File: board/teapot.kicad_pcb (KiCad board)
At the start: 2 copper layers, 50 x 50 mm, 15 parts, among them P1 BATT, P2 SMA, Q1 TEPT4400, U1 TLV61225, U2 microusb-b, U3 RFM69W, U4 STM32L052K8, U5 HTU21D, U6 MS5637, U7 SWD, U8 TPS79333DBVR

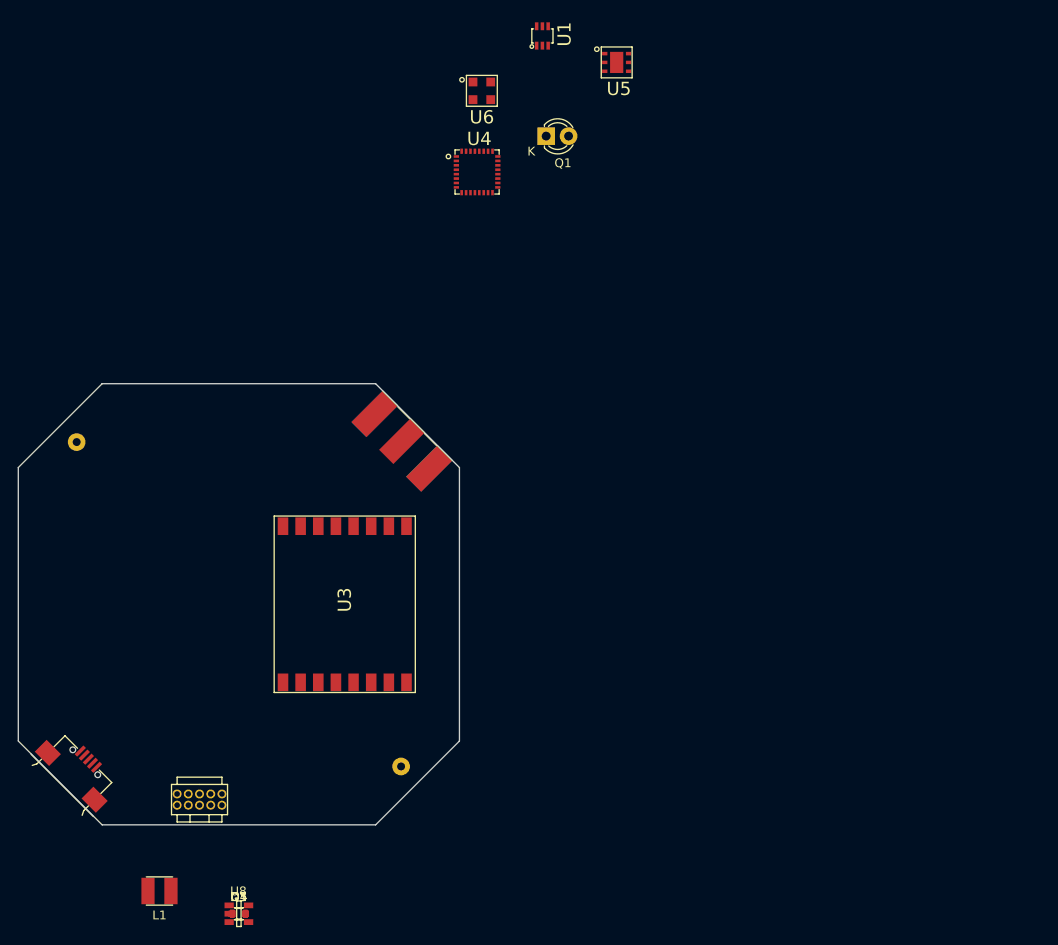
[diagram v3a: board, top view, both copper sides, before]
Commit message: Fixed a couple of footprint derps
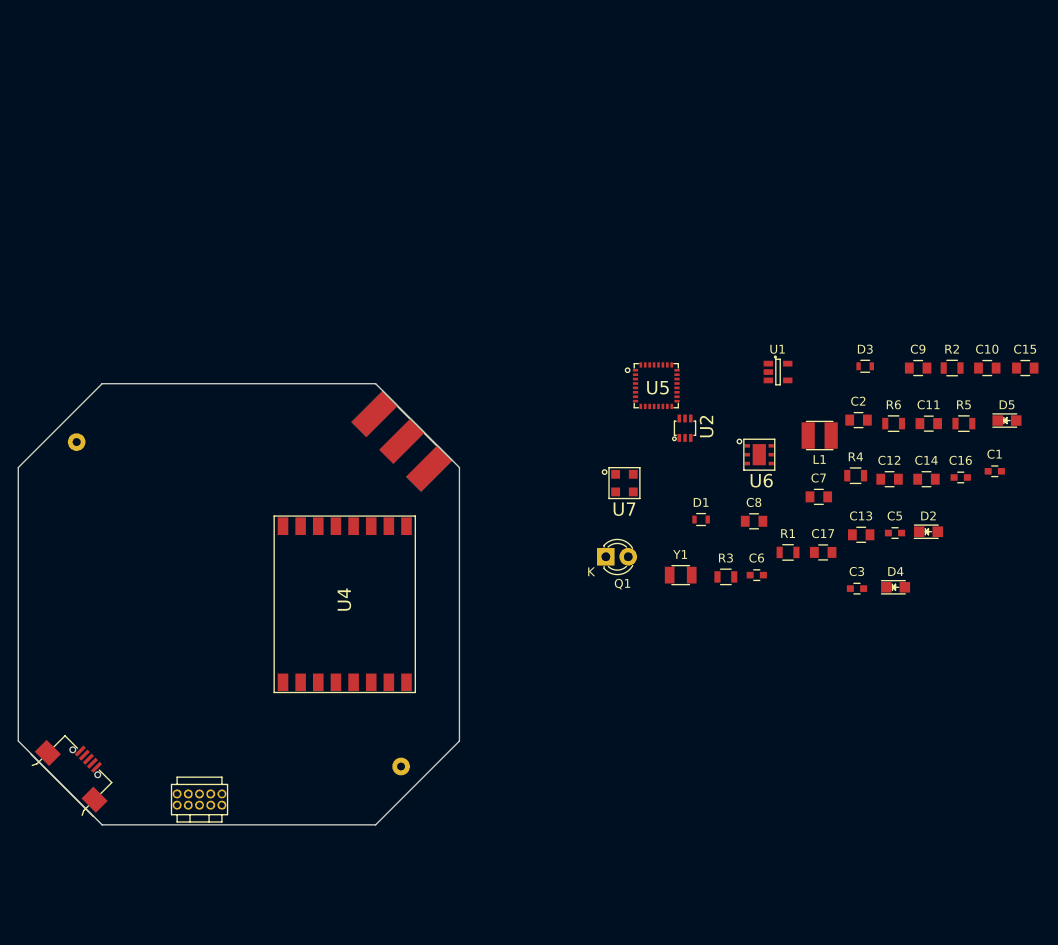
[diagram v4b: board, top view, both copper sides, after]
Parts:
- added C10: 100n, Capacitors_SMD:C_0805, F.Cu at (211.8, 86.2)
- added C11: 100n, Capacitors_SMD:C_0805, F.Cu at (205.2, 92.5)
- added C12: 1u, Capacitors_SMD:C_0805, F.Cu at (200.8, 98.8)
- added C13: 100n, Capacitors_SMD:C_0805, F.Cu at (197.5, 105.1)
- added C14: 100n, Capacitors_SMD:C_0805, F.Cu at (204.9, 98.8)
- added C15: 100n, Capacitors_SMD:C_0805, F.Cu at (216.1, 86.2)
- added C16: 10u, Capacitors_SMD:C_0603, F.Cu at (208.8, 98.6)
- added C17: 100n, Capacitors_SMD:C_0805, F.Cu at (193.2, 107.1)
- added C2: 100n, Capacitors_SMD:C_0805, F.Cu at (197.2, 92.1)
- added C3: 10u, Capacitors_SMD:C_0603, F.Cu at (197.1, 111.2)
- added C5: 10u, Capacitors_SMD:C_0603, F.Cu at (201.4, 104.9)
- added C6: 10u, Capacitors_SMD:C_0603, F.Cu at (185.7, 109.7)
- added C7: 100n, Capacitors_SMD:C_0805, F.Cu at (192.7, 100.8)
- added C8: 15p, Capacitors_SMD:C_0805, F.Cu at (185.4, 103.6)
- added C9: 15p, Capacitors_SMD:C_0805, F.Cu at (204.0, 86.2)
- added D2: RED, LEDs:LED-0805, F.Cu at (205.2, 104.8)
- added D4: GREEN, LEDs:LED-0805, F.Cu at (201.4, 111.1)
- added D5: YELLOW, LEDs:LED-0805, F.Cu at (214.1, 92.2)
- added R1: 1k, Resistors_SMD:R_0805, F.Cu at (189.2, 107.1)
- added R2: 10k, Resistors_SMD:R_0805, F.Cu at (207.8, 86.2)
- added R3: 10k, Resistors_SMD:R_0805, F.Cu at (182.2, 109.9)
- added R4: 1k, Resistors_SMD:R_0805, F.Cu at (196.9, 98.4)
- added R5: 1k, Resistors_SMD:R_0805, F.Cu at (209.2, 92.5)
- added R6: 10k, Resistors_SMD:R_0805, F.Cu at (201.2, 92.5)
- added Y1: 32.768k, footprints:XTAL_1206, F.Cu at (177.1, 109.7)
- moved C1 99.3 mm to (212.7, 97.9)
- moved D3 94.3 mm to (198.0, 86.0)
- moved L1 90.9 mm to (192.8, 93.9)
- moved U1 86.6 mm to (188.1, 86.7)
- moved D1 68.9 mm to (179.4, 103.4)
- moved Q1 48.2 mm to (168.6, 107.6)
- moved U2 47.3 mm to (177.6, 93.0)
- moved U7 47.3 mm to (170.7, 99.3)
- moved U6 47.3 mm to (186.0, 96.0)
- moved U5 31.6 mm to (174.3, 88.2)
- renumbered D4 to D1, D5 to D3, U8 to U1, U1 to U2, U2 to U3, U3 to U4, U4 to U5, U5 to U6, U6 to U7, U7 to U8
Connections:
- Q1 pad 1: (no net) -> /LIGHT
- U2 pad 2: (no net) -> Net-(C3-Pad1)
- U5 pad 2: (no net) -> Net-(C9-Pad1)
- U5 pad 3: (no net) -> Net-(C8-Pad1)
- U5 pad 5: (no net) -> Net-(C12-Pad1)

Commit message: Power consumption calculations
Resolves #5, resolves #2
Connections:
- net /LIGHT renamed /LIGHT_SENSE
- Q1 pad 2: +3V3 -> (no net)
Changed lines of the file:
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@@
 (kicad_pcb (version 4) (host pcbnew 4.0.1-3.201512150931+6195~38~ubuntu14.04.1-stable)
   (general
-    (links 91)
-    (no_connects 91)
+    (links 90)
+    (no_connects 90)
     (area 101.924999 87.924999 152.075001 138.075001)
     (thickness 1.6)
@@
   (net 19 "Net-(D4-Pad1)")
   (net 20 "Net-(D5-Pad1)")
-  (net 21 /LIGHT)
+  (net 21 /LIGHT_SENSE)
   (net_class Default "This is the default net class."
     (clearance 0.2)
@@
     (add_net /I2C_SCK)
     (add_net /I2C_SDA)
-    (add_net /LIGHT)
+    (add_net /LIGHT_SENSE)
     (add_net /SWCLK)
     (add_net /SWDIO)
@@
     )
     (pad 1 thru_hole rect (at 0 0 90) (size 2 2) (drill 1.00076) (layers *.Cu *.Mask F.SilkS)
-      (net 21 /LIGHT))
-    (pad 2 thru_hole circle (at 2.54 0) (size 2 2) (drill 1.00076) (layers *.Cu *.Mask F.SilkS)
-      (net 1 +3V3))
+      (net 21 /LIGHT_SENSE))
+    (pad 2 thru_hole circle (at 2.54 0) (size 2 2) (drill 1.00076) (layers *.Cu *.Mask F.SilkS))
     (model LEDs.3dshapes/LED-3MM.wrl
       (at (xyz 0.05 0 0))
@@
     (fp_line (start -0.6 -0.875) (end 0.6 -0.875) (layer F.SilkS) (width 0.15))
     (pad 1 smd rect (at -0.95 0) (size 0.7 1.3) (layers F.Cu F.Paste F.Mask)
-      (net 21 /LIGHT))
+      (net 21 /LIGHT_SENSE))
     (pad 2 smd rect (at 0.95 0) (size 0.7 1.3) (layers F.Cu F.Paste F.Mask)
       (net 3 GND))

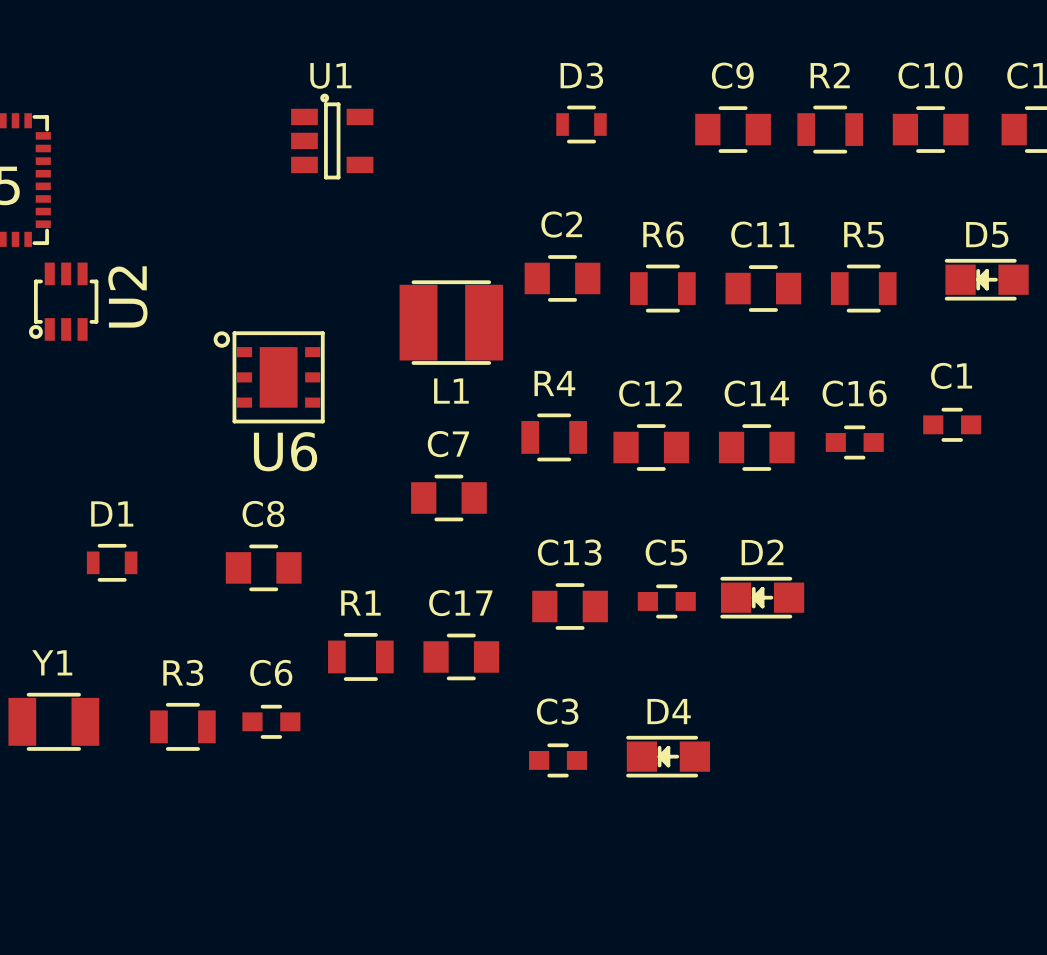
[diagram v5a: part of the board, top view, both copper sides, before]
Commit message: Added battery level monitor
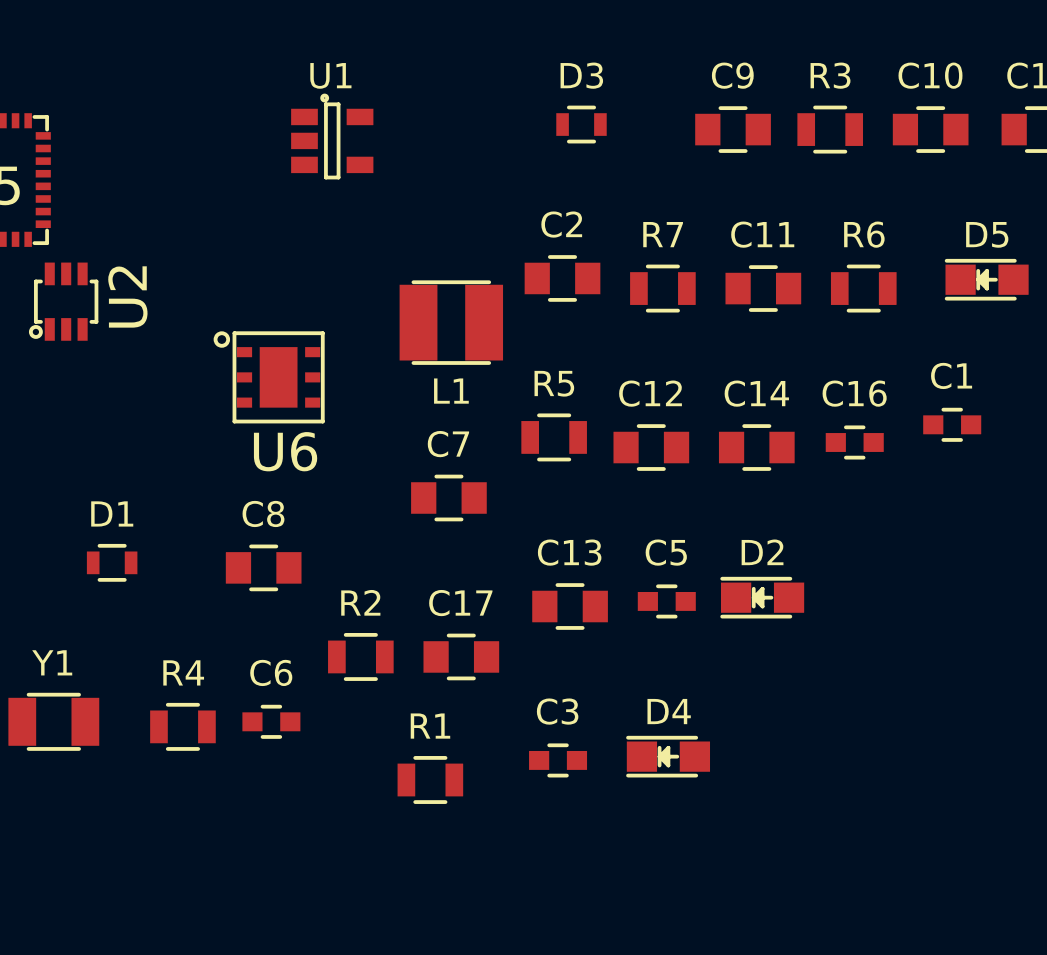
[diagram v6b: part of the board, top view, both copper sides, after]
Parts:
- added R1: 10k, Resistors_SMD:R_0805, F.Cu at (192.0, 112.0)
- renumbered R1 to R2, R2 to R3, R3 to R4, R4 to R5, R5 to R6, R6 to R7
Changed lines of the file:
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@@
 (kicad_pcb (version 4) (host pcbnew 4.0.1-3.201512150931+6195~38~ubuntu14.04.1-stable)
   (general
-    (links 90)
-    (no_connects 90)
+    (links 91)
+    (no_connects 91)
     (area 101.924999 87.924999 152.075001 138.075001)
     (thickness 1.6)
@@
     (tracks 0)
     (zones 0)
-    (modules 40)
+    (modules 41)
     (nets 22)
   )
@@
     (tags "resistor 0805")
     (attr smd)
-    (fp_text reference R1 (at 0 -2.1) (layer F.SilkS)
+    (fp_text reference R2 (at 0 -2.1) (layer F.SilkS)
       (effects (font (size 1 1) (thickness 0.15)))
     )
@@
     (tags "resistor 0805")
     (attr smd)
-    (fp_text reference R2 (at 0 -2.1) (layer F.SilkS)
+    (fp_text reference R3 (at 0 -2.1) (layer F.SilkS)
       (effects (font (size 1 1) (thickness 0.15)))
     )
@@
     (tags "resistor 0805")
     (attr smd)
-    (fp_text reference R3 (at 0 -2.1) (layer F.SilkS)
+    (fp_text reference R4 (at 0 -2.1) (layer F.SilkS)
       (effects (font (size 1 1) (thickness 0.15)))
     )
@@
     (tags "resistor 0805")
     (attr smd)
-    (fp_text reference R4 (at 0 -2.1) (layer F.SilkS)
+    (fp_text reference R5 (at 0 -2.1) (layer F.SilkS)
       (effects (font (size 1 1) (thickness 0.15)))
     )
@@
     (tags "resistor 0805")
     (attr smd)
-    (fp_text reference R5 (at 0 -2.1) (layer F.SilkS)
+    (fp_text reference R6 (at 0 -2.1) (layer F.SilkS)
       (effects (font (size 1 1) (thickness 0.15)))
     )
@@
     (tags "resistor 0805")
     (attr smd)
-    (fp_text reference R6 (at 0 -2.1) (layer F.SilkS)
+    (fp_text reference R7 (at 0 -2.1) (layer F.SilkS)
       (effects (font (size 1 1) (thickness 0.15)))
     )
@@
       (at (xyz 0 0 0))
       (scale (xyz 1 1 1))
+      (rotate (xyz 0 0 0))
+    )
+  )
+  (module Resistors_SMD:R_0805 (layer F.Cu)
+    (at 192 112)
+    (descr "Resistor SMD 0805, reflow soldering, Vishay (see dcrcw.pdf)")
+    (tags "resistor 0805")
+    (attr smd)
+    (fp_text reference R1 (at 0 -2.1) (layer F.SilkS)
+      (effects (font (size 1 1) (thickness 0.15)))
+    )
+    (fp_text value 10k (at 0 2.1) (layer F.Fab)
+      (effects (font (size 1 1) (thickness 0.15)))
+    )
+    (fp_line (start -1.6 -1) (end 1.6 -1) (layer F.CrtYd) (width 0.05))
+    (fp_line (start -1.6 1) (end 1.6 1) (layer F.CrtYd) (width 0.05))
+    (fp_line (start -1.6 -1) (end -1.6 1) (layer F.CrtYd) (width 0.05))
+    (fp_line (start 1.6 -1) (end 1.6 1) (layer F.CrtYd) (width 0.05))
+    (fp_line (start 0.6 0.875) (end -0.6 0.875) (layer F.SilkS) (width 0.15))
+    (fp_line (start -0.6 -0.875) (end 0.6 -0.875) (layer F.SilkS) (width 0.15))
+    (pad 1 smd rect (at -0.95 0) (size 0.7 1.3) (layers F.Cu F.Paste F.Mask)
+      (net 2 "Net-(C1-Pad1)"))
+    (pad 2 smd rect (at 0.95 0) (size 0.7 1.3) (layers F.Cu F.Paste F.Mask))
+    (model Resistors_SMD.3dshapes/R_0805.wrl
+      (at (xyz 0 0 0))
+      (scale (xyz 1 1 1))

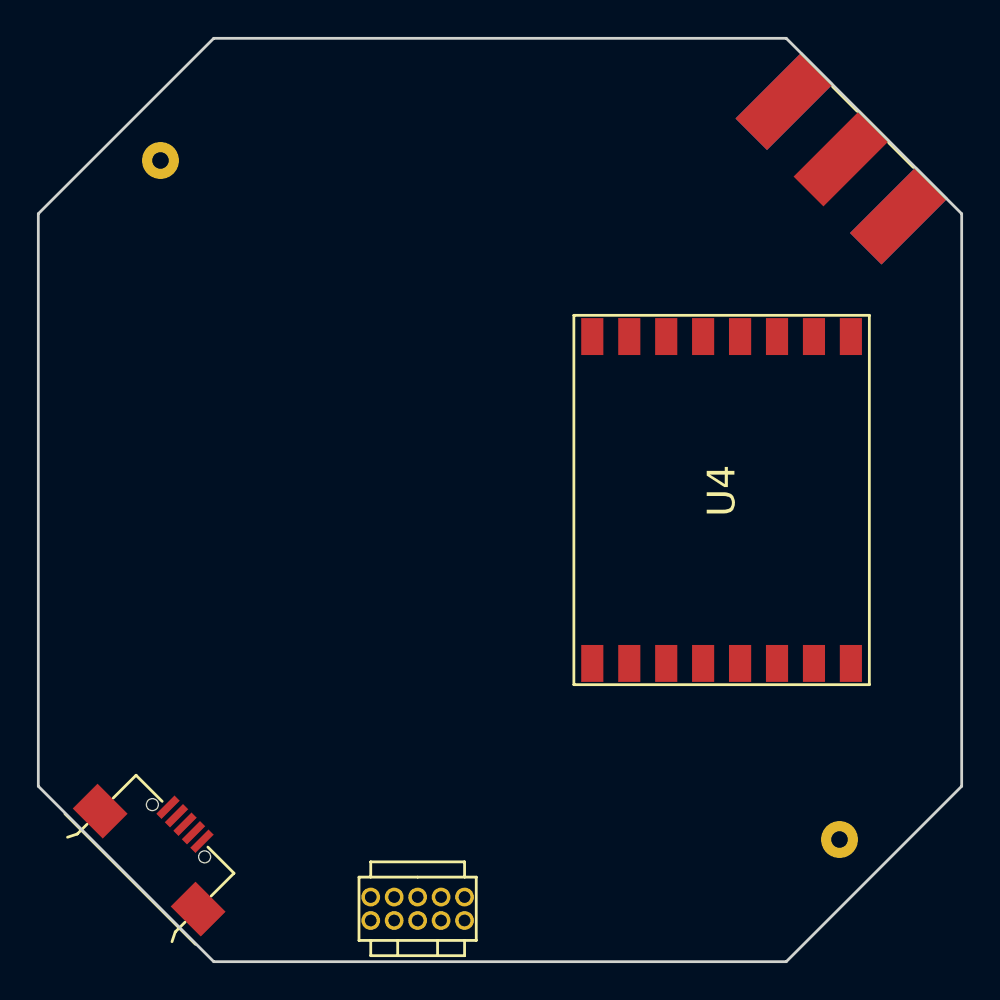
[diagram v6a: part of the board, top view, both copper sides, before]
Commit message: added mounting holes. resolves #8
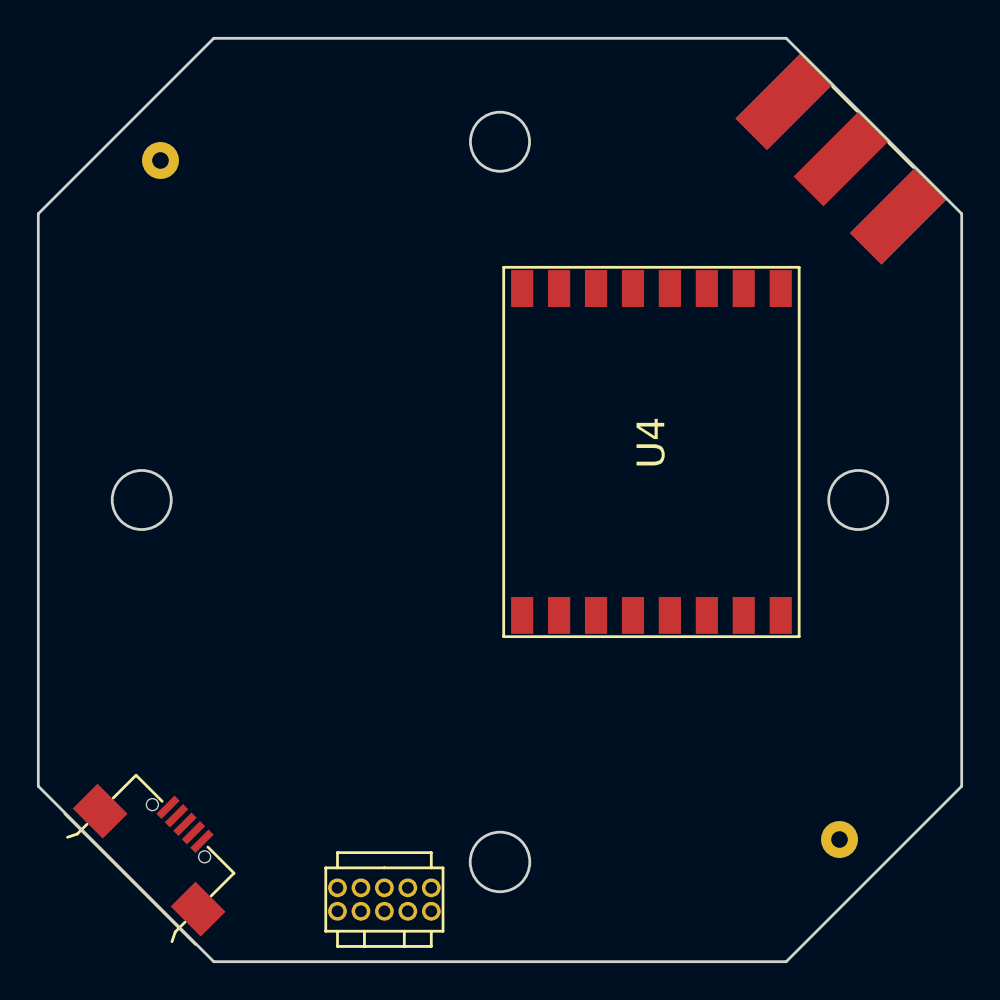
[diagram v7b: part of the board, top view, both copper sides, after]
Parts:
- moved U4 4.60 mm to (135.2, 110.4)
- moved U8 1.87 mm to (118.2, 134.0)
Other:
- outline, holes or cut-outs redrawn
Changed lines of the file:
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@@
     (links 91)
     (no_connects 91)
-    (area 101.924999 87.924999 152.075001 138.075001)
+    (area 100.562048 83 218.291905 139.437952)
     (thickness 1.6)
-    (drawings 8)
+    (drawings 16)
     (tracks 0)
     (zones 0)
@@
   )
   (module footprints:RFM69 (layer F.Cu)
-    (at 139 113 90)
+    (at 135.2 110.4 90)
     (fp_text reference U4 (at 0.5 0 90) (layer F.SilkS)
       (effects (font (size 1.5 1.5) (thickness 0.15)))
@@
   )
   (module footprints:SWD (layer F.Cu)
-    (at 120 134.5)
+    (at 118.2 134)
     (fp_text reference U8 (at 2.5 -2.9) (layer F.SilkS) hide
       (effects (font (size 1 1) (thickness 0.15)))
@@
     )
   )
+  (gr_circle (center 146.4 113) (end 148.8 113) (layer F.CrtYd) (width 0.2))
+  (gr_circle (center 127 93.6) (end 129.4 93.6) (layer F.CrtYd) (width 0.2))
+  (gr_circle (center 107.6 113) (end 110 113) (layer F.CrtYd) (width 0.2))
+  (gr_circle (center 127 132.6) (end 129.4 132.6) (layer F.CrtYd) (width 0.2))
+  (gr_circle (center 127 132.6) (end 128.6 132.4) (layer Edge.Cuts) (width 0.15))
+  (gr_circle (center 146.4 113) (end 148 113) (layer Edge.Cuts) (width 0.15))
+  (gr_circle (center 127 93.6) (end 128.6 93.6) (layer Edge.Cuts) (width 0.15))
+  (gr_circle (center 107.6 113) (end 109.2 113) (layer Edge.Cuts) (width 0.15))
   (gr_line (start 102 128.5) (end 111.5 138) (angle 90) (layer Edge.Cuts) (width 0.15))
   (gr_line (start 102 97.5) (end 102 128.5) (angle 90) (layer Edge.Cuts) (width 0.15))
